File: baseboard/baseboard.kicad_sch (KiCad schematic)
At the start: 19 parts, among them IC1 ATA6561-GAQW-N, IC2 NJM2845DL1-33-TE1, J10 Conn_01x01_Pin, J9 A295-CTRPB-1, U1 PY32E407V1xT_START

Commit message: schematics
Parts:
- added J4, J5: ~, kicad8-2:Pmod_socket, symbol kicad8-2:Pmod_Socket
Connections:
- net ETH_RMII_CRS_DV: now also J4.7 (Pin_7)
- net ETH_RMII_REF_CLK: now also J4.1 (Pin_1)
- net ETH_RMII_RXD0: now also J4.2 (Pin_2)
- net ETH_RMII_RXD1: now also J4.8 (Pin_8)
- net ETH_RMII_TXD0: now also J4.9 (Pin_9)
- net ETH_RMII_TXD1: now also J4.4 (Pin_4)
- net ETH_RMII_TX_EN: now also J4.3 (Pin_3)

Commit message: schematics can
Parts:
- added C3: 4.7n, Capacitor_SMD:C_0603_1608Metric_Pad1.08x0.95mm_HandSolder, symbol Device:C
- added D5: SM24CANB-02HTG, samacsys:SM24CANB02HTG, symbol samacsys:SM24CANB-02HTG
- added J11, J8: Conn_01x02_Pin, Connector_PinHeader_2.54mm:PinHeader_1x02_P2.54mm_Vertical, symbol Connector:Conn_01x02_Pin
- added J6: Screw_Terminal_01x02, TerminalBlock_Phoenix:TerminalBlock_Phoenix_MKDS-1,5-2-5.08_1x02_P5.08mm_Horizontal, symbol Connector:Screw_Terminal_01x02
- added L1: SDCW3216-2-222TF, samacsys:SDCW32162222TF, symbol samacsys:SDCW3216-2-222TF
- added R1, R2: 60.4, Resistor_SMD:R_0603_1608Metric_Pad0.98x0.95mm_HandSolder, symbol Device:R
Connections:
- net CANH: now also L1.4
- net CANL: now also L1.1
- net GND: now also C3.2, D5.3
- new net: J11.1 (Pin_1), R2.1
- new net: D5.2, J11.2 (Pin_2), J6.1 (Pin_1), L1.3
- new net: D5.1, J6.2 (Pin_2), J8.1 (Pin_1), L1.2
- new net: C3.1, R1.1, R2.2
- new net: J8.2 (Pin_2), R1.2
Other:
- moved on the sheet: J1, J2, J3

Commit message: edit schematics
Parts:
- added J7: Conn_02x25_Odd_Even, Connector_PinHeader_2.54mm:PinHeader_2x25_P2.54mm_Vertical, symbol Connector_Generic:Conn_02x25_Odd_Even
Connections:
- net ETH_MDC: now also J5.2 (Pin_2)
- net ETH_MDIO: now also J5.1 (Pin_1)
- net Pmod1_1: now also U1.97 (E0)
- net Pmod1_2: now also U1.98 (E1)
- net Pmod1_3: now also U1.1 (E2)
- net Pmod1_4: now also U1.2 (E3)
- net Pmod1_5: now also U1.3 (E4)
- net Pmod1_6: now also U1.4 (E5)
- net Pmod1_7: now also U1.5 (E6)
- net Pmod1_8: now also U1.38 (E7)
- net Pmod2_1: now also U1.39 (E8)
- net Pmod2_2: now also U1.40 (E9)
- net Pmod2_3: now also U1.41 (E10)
- net Pmod2_4: now also U1.42 (E11)
- net Pmod2_5: now also U1.46 (E15)
- net Pmod2_6: now also U1.45 (E14)
- net Pmod2_7: now also U1.44 (E13)
- net Pmod2_8: now also U1.43 (E12)
- net Pmod3_1: now also U1.34 (B2)
- net Pmod3_2: now also U1.90 (B3)
- net Pmod3_3: now also U1.91 (B4)
- net Pmod3_4: now also U1.92 (B5)
- net Pmod3_5: now also U1.96 (B9)
- net Pmod3_6: now also U1.95 (B8)
- net Pmod3_7: now also U1.94 (B7)
- net Pmod3_8: now also U1.93 (B6)

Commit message: edit schematics
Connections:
- net Pmod1_8: now also U1.45 (E14); no longer U1.38 (E7)
- net Pmod2_1: now also U1.11 (F4); no longer U1.39 (E8)
- net Pmod2_2: now also U1.19 (F2); no longer U1.40 (E9)
- net Pmod2_3: now also U1.46 (E15); no longer U1.41 (E10)
- net Pmod2_4: now also U1.62 (D15); no longer U1.42 (E11)
- net Pmod2_5: now also U1.71 (A10); no longer U1.46 (E15)
- net Pmod2_6: now also U1.79 (C10); no longer U1.45 (E14)
- net Pmod2_7: now also U1.81 (C12); no longer U1.44 (E13)
- net Pmod2_8: now also U1.84 (D2); no longer U1.43 (E12)
- net Pmod3_1: now also U1.85 (D3); no longer U1.34 (B2)
- net Pmod3_2: now also U1.86 (D4); no longer U1.90 (B3)
- net Pmod3_3: now also U1.87 (D5); no longer U1.91 (B4)
- net Pmod3_4: now also U1.88 (D6); no longer U1.92 (B5)
- net Pmod3_5: now also U1.89 (D7); no longer U1.96 (B9)
- net Pmod3_6: now also U1.90 (B3); no longer U1.95 (B8)
- net Pmod3_7: now also U1.91 (B4); no longer U1.94 (B7)
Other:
- note added: "FT"

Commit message: schematics
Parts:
- added J12: ~, kicad8-2:Pmod_socket, symbol kicad8-2:Pmod_Socket
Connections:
- net +3V3: now also J12.12 (Pin_12), J12.6 (Pin_6)
- net GND: now also J12.11 (Pin_11), J12.5 (Pin_5)
- net Pmod4_1: now reaches U1.34 (B2)
- net Pmod4_1: now also J12.1 (Pin_1)
- net Pmod4_2: now reaches U1.38 (E7)
- net Pmod4_2: now also J12.2 (Pin_2)
- net Pmod4_3: now reaches U1.39 (E8)
- net Pmod4_3: now also J12.3 (Pin_3)
- net Pmod4_4: now reaches U1.40 (E9)
- net Pmod4_4: now also J12.4 (Pin_4)
- net Pmod4_5: now reaches U1.41 (E10)
- net Pmod4_5: now also J12.10 (Pin_10)
- net Pmod4_6: now reaches U1.42 (E11)
- net Pmod4_6: now also J12.9 (Pin_9)
- net Pmod4_7: now reaches U1.43 (E12)
- net Pmod4_7: now also J12.8 (Pin_8)
- net Pmod4_8: now reaches U1.44 (E13)
- net Pmod4_8: now also J12.7 (Pin_7)
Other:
- note added: "TTa"
- moved on the sheet: C3, D5, IC1, J11, J6, J7, J8, L1, R1, R2

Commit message: schematics
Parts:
- added J13: Conn_02x05_Odd_Even, Connector_PinHeader_2.54mm:PinHeader_2x05_P2.54mm_Vertical, symbol Connector_Generic:Conn_02x05_Odd_Even
- added J14: Conn_02x25_Odd_Even, Connector_PinHeader_2.54mm:PinHeader_2x25_P2.54mm_Vertical, symbol Connector_Generic:Conn_02x25_Odd_Even
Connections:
- net +3V3: now also J7.14 (Pin_14), J7.25 (Pin_25), J7.50 (Pin_50), J13.4 (Pin_4), J14.24 (Pin_24), J14.49 (Pin_49)
- net ETH_MDC: now also J14.16 (Pin_16)
- net ETH_MDIO: now also J14.21 (Pin_21)
- net ETH_RMII_CRS_DV: now also J7.5 (Pin_5)
- net ETH_RMII_REF_CLK: now also J14.22 (Pin_22)
- net ETH_RMII_RXD0: now also J7.6 (Pin_6)
- net ETH_RMII_RXD1: now also J7.7 (Pin_7)
- net ETH_RMII_TXD0: now also J7.1 (Pin_1)
- net ETH_RMII_TXD1: now also J7.2 (Pin_2)
- net ETH_RMII_TX_EN: now also J14.50 (Pin_50)
- net GND: now also J7.13 (Pin_13), J7.24 (Pin_24), J7.49 (Pin_49), J13.10 (Pin_10), J13.2 (Pin_2), J14.23 (Pin_23), J14.48 (Pin_48)
- net Pmod1_1: now also J7.47 (Pin_47)
- net Pmod1_2: now also J7.48 (Pin_48)
- net Pmod1_3: now also J14.1 (Pin_1)
- net Pmod1_4: now also J14.2 (Pin_2)
- net Pmod1_5: now also J14.3 (Pin_3)
- net Pmod1_6: now also J14.4 (Pin_4)
- net Pmod1_7: now also J14.5 (Pin_5)
- net Pmod1_8: now also J14.45 (Pin_45)
- net Pmod2_1: now also J14.11 (Pin_11)
- net Pmod2_2: now also J14.19 (Pin_19)
- net Pmod2_3: now also J14.46 (Pin_46)
- net Pmod2_4: now also J7.12 (Pin_12)
- net Pmod2_5: now also J7.21 (Pin_21)
- net Pmod2_6: now also J7.29 (Pin_29)
- net Pmod2_7: now also J7.31 (Pin_31)
- net Pmod2_8: now also J7.34 (Pin_34)
- net Pmod3_1: now also J7.35 (Pin_35)
- net Pmod3_2: now also J7.36 (Pin_36)
- net Pmod3_3: now also J7.37 (Pin_37)
- net Pmod3_4: now also J7.38 (Pin_38)
- net Pmod3_5: now also J7.39 (Pin_39)
- net Pmod3_6: now also J7.41 (Pin_41), U1.91 (B4); no longer U1.90 (B3)
- net Pmod3_7: now also J7.42 (Pin_42), U1.92 (B5); no longer U1.91 (B4)
- net Pmod3_8: now also J7.43 (Pin_43)
- net Pmod4_1: now also J14.34 (Pin_34)
- net Pmod4_2: now also J14.38 (Pin_38)
- net Pmod4_3: now also J14.39 (Pin_39)
- net Pmod4_4: now also J14.40 (Pin_40)
- net Pmod4_5: now also J14.41 (Pin_41)
- net Pmod4_6: now also J14.42 (Pin_42)
- net Pmod4_7: now also J14.43 (Pin_43)
- net Pmod4_8: now also J14.44 (Pin_44)
- net CAN_TXD: now reaches IC1.1 (TXD), U1.83 (D1)
- net CAN_TXD: now also J7.33 (Pin_33)
- net CAN_RXD: now reaches IC1.4 (RXD), U1.82 (D0)
- net CAN_RXD: now also J7.32 (Pin_32)
- net D13: now reaches IC1.8 (STBY), U1.60 (D13)
- net D13: now also J7.10 (Pin_10)
- net D14: now reaches J7.11 (Pin_11)
- net D14: now also U1.61 (D14)
- net C6: now reaches J7.15 (Pin_15)
- net C6: now also U1.65 (C6)
- net C7: now reaches J7.16 (Pin_16)
- net C7: now also U1.66 (C7)
- net C8: now reaches J7.17 (Pin_17)
- net C8: now also U1.67 (C8)
- net C9: now reaches J7.18 (Pin_18)
- net C9: now also U1.68 (C9)
- net A8: now reaches J7.19 (Pin_19)
- net A8: now also U1.69 (A8)
- net A9: now reaches J7.20 (Pin_20)
- net A9: now also U1.70 (A9)
- net A11: now reaches J7.22 (Pin_22)
- net A11: now also U1.72 (A11)
- net A12: now reaches J7.23 (Pin_23)
- net A12: now also U1.73 (A12)
- net JTMS: now reaches J7.26 (Pin_26)
- net JTMS: now also U1.76 (A13), J13.5 (Pin_5)
- net JTCK: now reaches J7.27 (Pin_27)
- net JTCK: now also U1.77 (A14), J13.1 (Pin_1)
- net JTDI: now reaches J7.28 (Pin_28)
- net JTDI: now also U1.78 (A15), J13.9 (Pin_9)
- net B14: now reaches J7.3 (Pin_3)
- net B14: now also U1.53 (B14)
- net C11: now reaches J7.30 (Pin_30)
- net C11: now also U1.80 (C11)
- net B15: now reaches J7.4 (Pin_4)
- net B15: now also U1.54 (B15)
- net JTDO: now reaches J7.40 (Pin_40)
- net JTDO: now also U1.90 (B3), J13.3 (Pin_3)
- net B7: now reaches J7.44 (Pin_44)
- net B7: now also U1.94 (B7)
- net B8: now reaches J7.45 (Pin_45)
- net B8: now also U1.95 (B8)
- net B9: now reaches J7.46 (Pin_46)
- net B9: now also U1.96 (B9)
- net D11: now reaches J7.8 (Pin_8)
- net D11: now also U1.58 (D11)
- net D12: now reaches J7.9 (Pin_9)
- net D12: now also U1.59 (D12)
- net F3: now reaches U1.10 (F3)
- net F3: now also J14.10 (Pin_10)
- net F0: now reaches U1.12 (F0)
- net F0: now also J14.12 (Pin_12)
- net F1: now reaches U1.13 (F1)
- net F1: now also J14.13 (Pin_13)
- net F5: now reaches U1.14 (F5)
- net F5: now also J14.14 (Pin_14)
- net C0: now reaches U1.15 (C0)
- net C0: now also J14.15 (Pin_15)
- net C2: now reaches U1.17 (C2)
- net C2: now also J14.17 (Pin_17)
- net C3: now reaches U1.18 (C3)
- net C3: now also J14.18 (Pin_18)
- net A0: now reaches U1.20 (A0)
- net A0: now also J14.20 (Pin_20)
- net A3: now reaches U1.25 (A3)
- net A3: now also J14.25 (Pin_25)
- net A4: now reaches U1.26 (A4)
- net A4: now also J14.26 (Pin_26)
- net A5: now reaches U1.27 (A5)
- net A5: now also J14.27 (Pin_27)
- net A6: now reaches U1.28 (A6)
- net A6: now also J14.28 (Pin_28)
- net A7: now reaches U1.29 (A7)
- net A7: now also J14.29 (Pin_29)
- net C4: now reaches U1.30 (C4)
- net C4: now also J14.30 (Pin_30)
- net C5: now reaches U1.31 (C5)
- net C5: now also J14.31 (Pin_31)
- net B0: now reaches U1.32 (B0)
- net B0: now also J14.32 (Pin_32)
- net B1: now reaches U1.33 (B1)
- net B1: now also J14.33 (Pin_33)
- net VSSA: now reaches U1.35 (VSSA)
- net VSSA: now also J14.35 (Pin_35)
- net VREF+: now reaches U1.36 (VREF+)
- net VREF+: now also J14.36 (Pin_36)
- net VCCA: now reaches U1.37 (VCCA)
- net VCCA: now also J14.37 (Pin_37)
- net B10: now reaches U1.47 (B10)
- net B10: now also J14.47 (Pin_47)
- net VBAT: now reaches U1.6 (VBAT)
- net VBAT: now also J14.6 (Pin_6)
- net C13: now reaches U1.7 (C13)
- net C13: now also J14.7 (Pin_7)
- net C14: now reaches U1.8 (C14)
- net C14: now also J14.8 (Pin_8)
- net C15: now reaches U1.9 (C15)
- net C15: now also J14.9 (Pin_9)
- no-connect marks 0 -> 3
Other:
- moved on the sheet: J7

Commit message: 0907
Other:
- moved on the sheet: C1, C2, C3, D1, D2, D3, D4, D5, IC1, IC2, J1, J10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

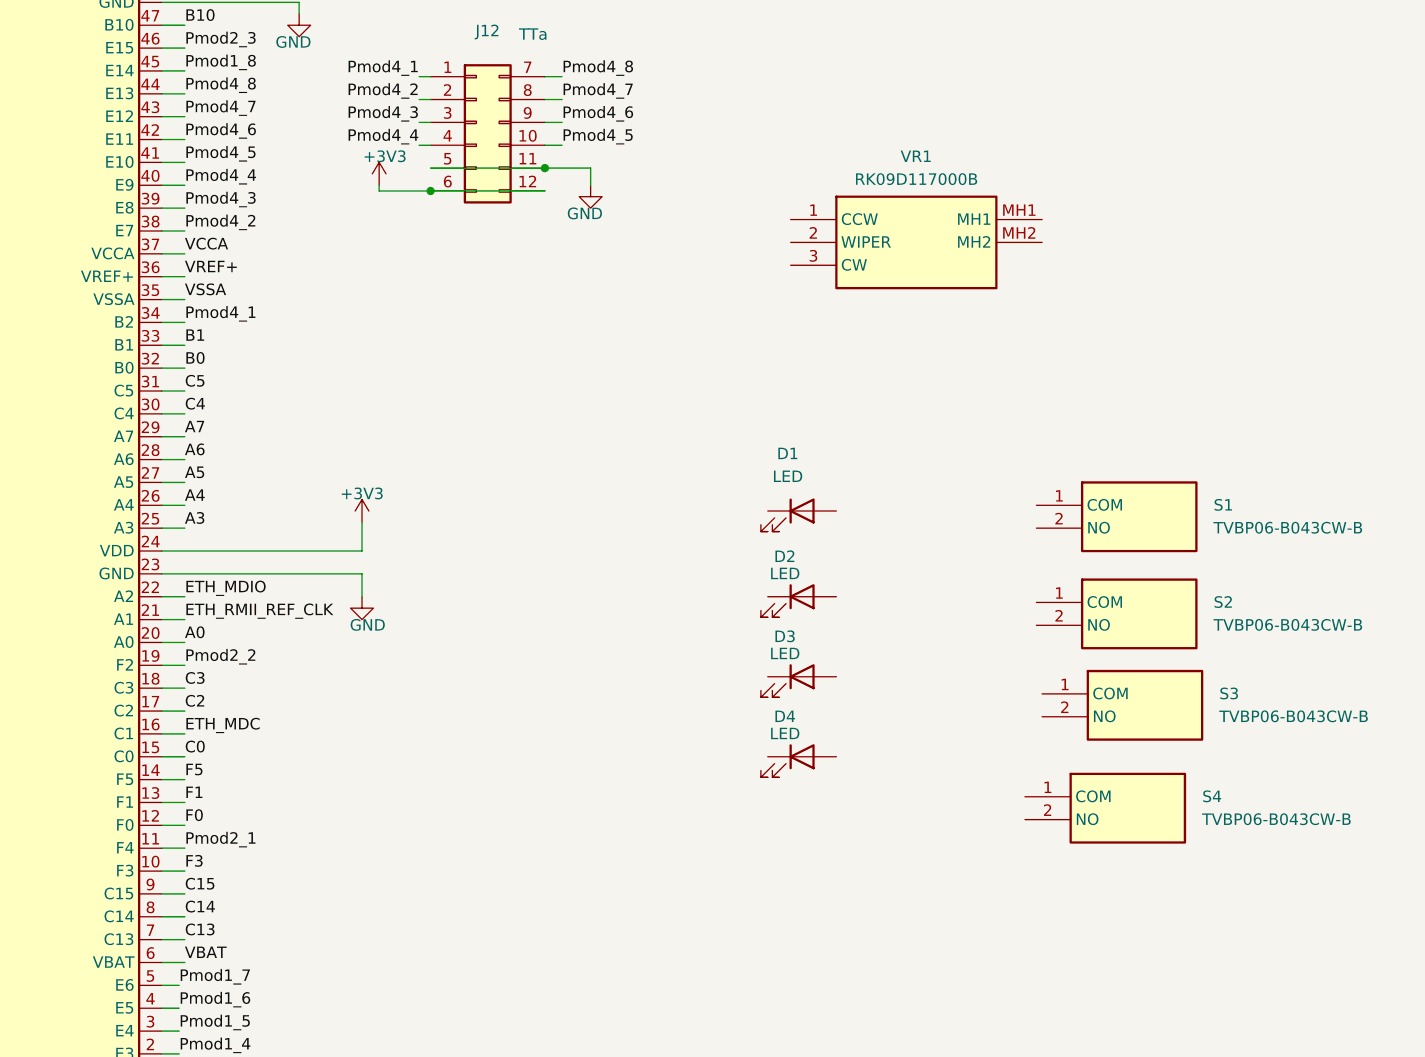
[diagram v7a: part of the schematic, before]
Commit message: schematics update
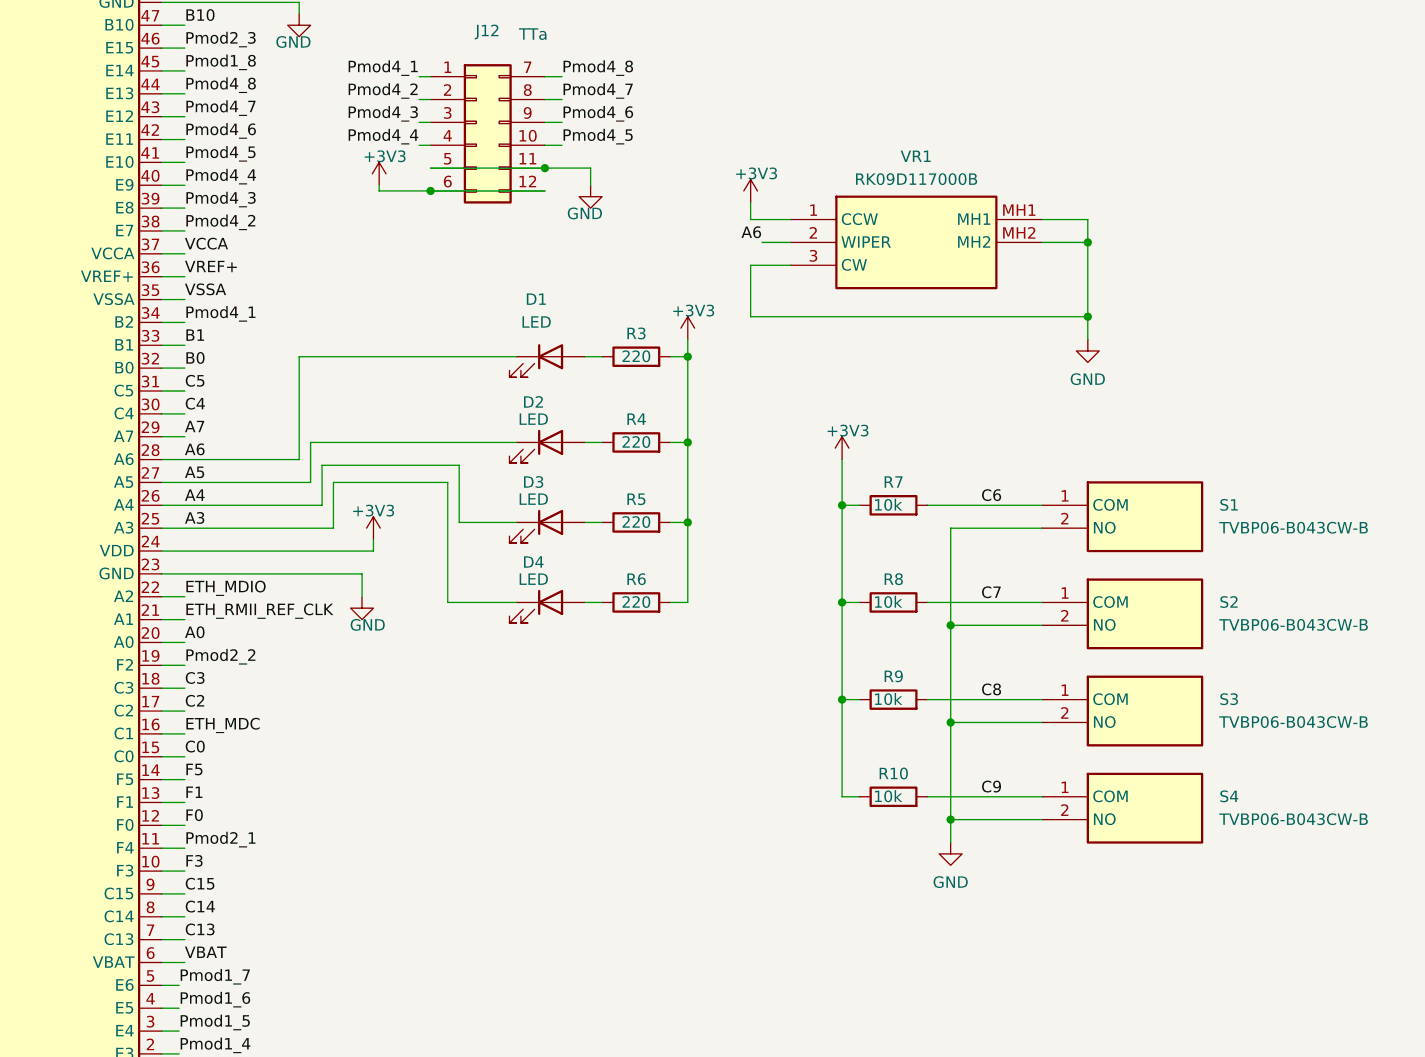
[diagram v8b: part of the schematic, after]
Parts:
- added R10, R7, R8, R9: 10k, Resistor_SMD:R_0603_1608Metric_Pad0.98x0.95mm_HandSolder, symbol Device:R
- added R3, R4, R5, R6: 220, Resistor_SMD:R_0603_1608Metric_Pad0.98x0.95mm_HandSolder, symbol Device:R
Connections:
- net +3V3: now also VR1.1 (CCW), R10.1, R3.2, R4.2, R5.2, R6.2, R7.1, R8.1, R9.1
- net A3: now also D4.1 (K)
- net A4: now also D3.1 (K)
- net A5: now also D2.1 (K)
- net A6: now also D1.1 (K), VR1.2 (WIPER)
- net C6: now also S1.1 (COM), R7.2
- net C7: now also S2.1 (COM), R8.2
- net C8: now also S3.1 (COM), R9.2
- net C9: now also S4.1 (COM), R10.2
- net GND: now also S1.2 (NO), S2.2 (NO), S3.2 (NO), S4.2 (NO), VR1.3 (CW), VR1.MH1, VR1.MH2
- net at D1.2 (A): now also R3.1
- net at D2.2 (A): now also R4.1
- net at D4.2 (A): now also R6.1
- net at D3.2 (A): now also R5.1
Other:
- moved on the sheet: D1, D2, D3, D4, S1, S2, S3, S4
